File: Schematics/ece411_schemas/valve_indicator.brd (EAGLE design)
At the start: 85.1 x 53.6 mm, 82 parts, among them T1 2N2222, T2 2N2222, T3 2N2222, T4 2N2222, U1 AZ34063UMTR-G1, U2 AZ34063UMTR-G1, U3 STM32F042K6

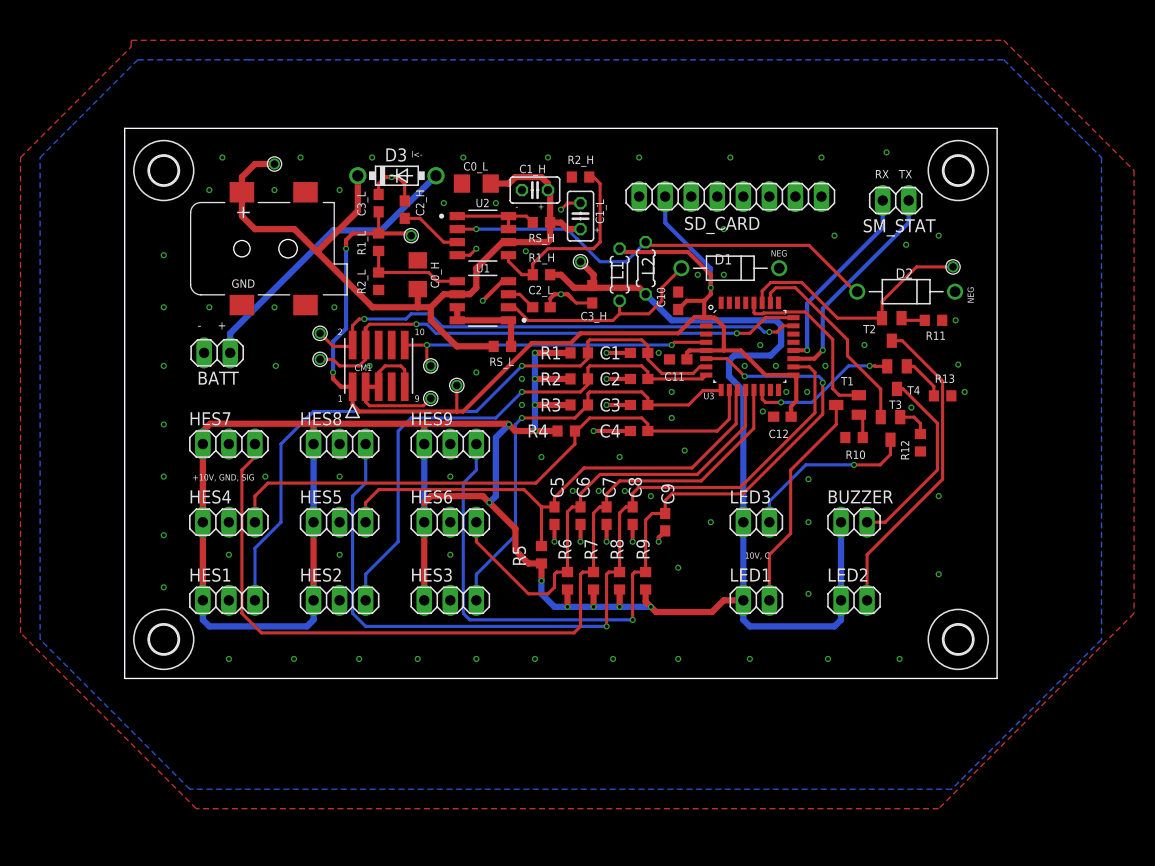
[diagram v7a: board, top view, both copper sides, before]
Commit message: updated board given feedback
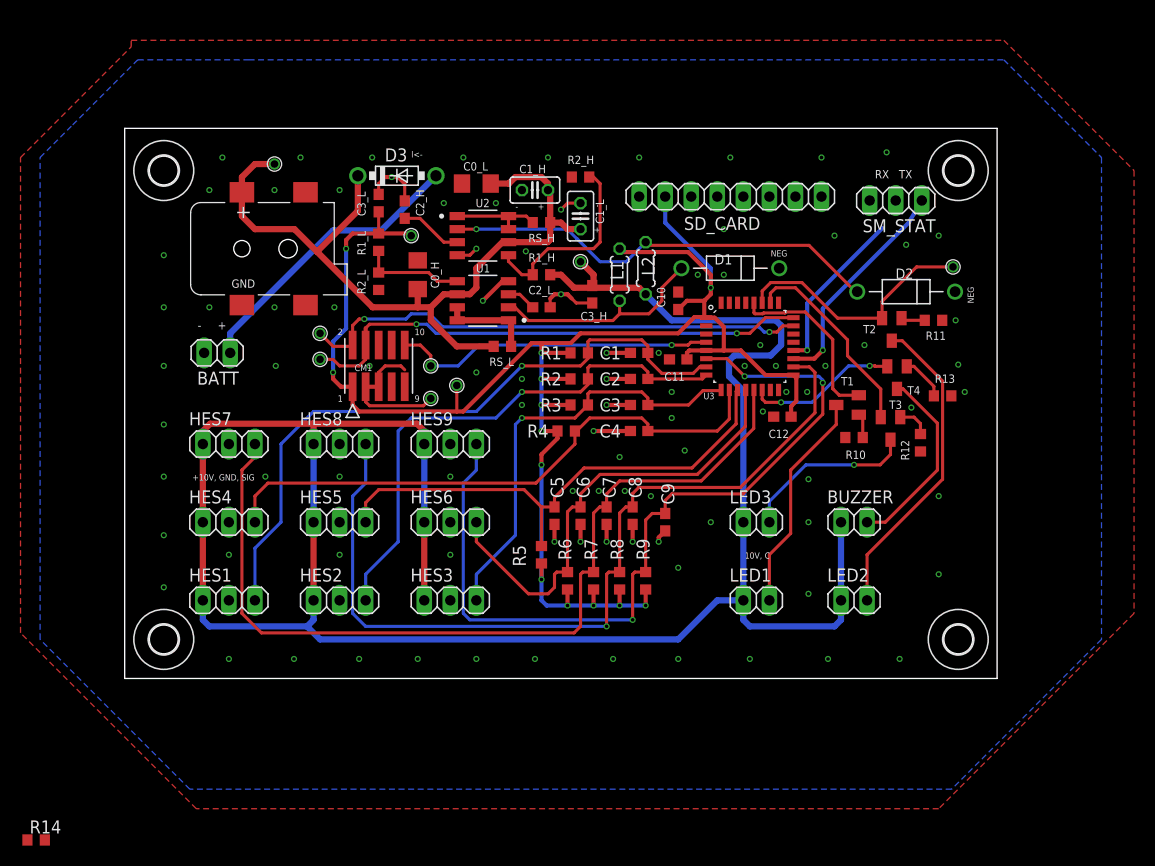
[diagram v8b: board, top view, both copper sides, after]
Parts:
- added R14: 10k, rcl:R0603
- SM_STAT: device pinhead:1X02 -> pinhead:1X03
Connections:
- removed net N$23: CM1.3, CM1.5, CM1.9, TPJGND.1
- new net N$1: R14.1, SM_STAT.2
- net +10V: no longer R1.1, R2.1, R3.1, R4.1, R5.1, R6.1, R7.1, R8.1, R9.1
- net +3V3: now also R1.1, R2.1, R3.1, R4.1, R5.1, R6.1, R7.1, R8.1, R9.1
- net GND: now also CM1.3, CM1.5, CM1.9, SM_STAT.3, TPJGND.1
- net UART-RX: now also R14.2; no longer SM_STAT.2
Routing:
- net +3V3: track 117.0 -> 171.0 mm, vias 3 -> 13
- net +10V: track 256.8 -> 212.9 mm, vias 11 -> 0
- net N$23: track 15.6 -> 0.00 mm
- net GND: track 37.5 -> 51.4 mm, vias 96 -> 95
- net UART-RX: track 19.0 -> 16.3 mm
- net N$32: track 31.7 -> 31.8 mm, vias 2 -> 1
